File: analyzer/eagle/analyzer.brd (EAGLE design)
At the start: 33 x 38.1 mm, 34 parts, among them J4 USBSMD, U1 ATA6631, U2 FT232RL, U3 ATMEGA328, X1 16MHz

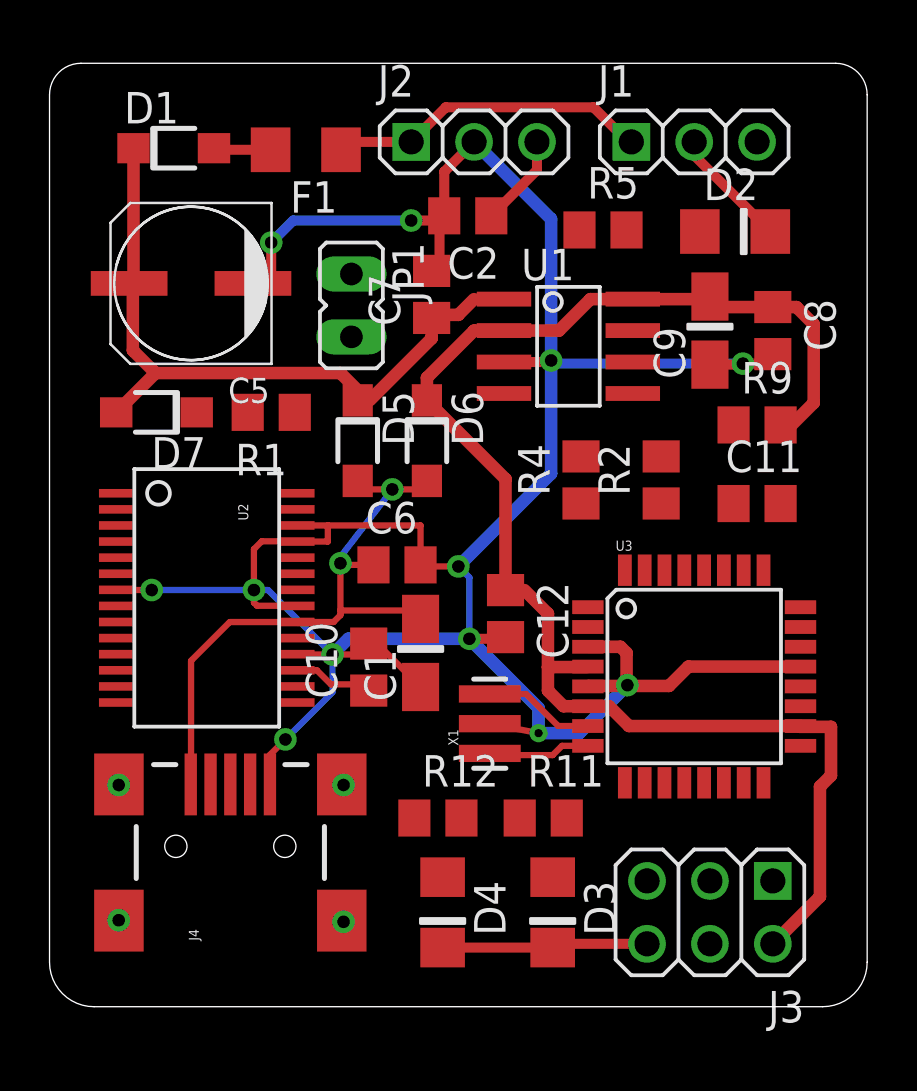
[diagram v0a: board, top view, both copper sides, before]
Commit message: Completed the routing of the analyzer board.
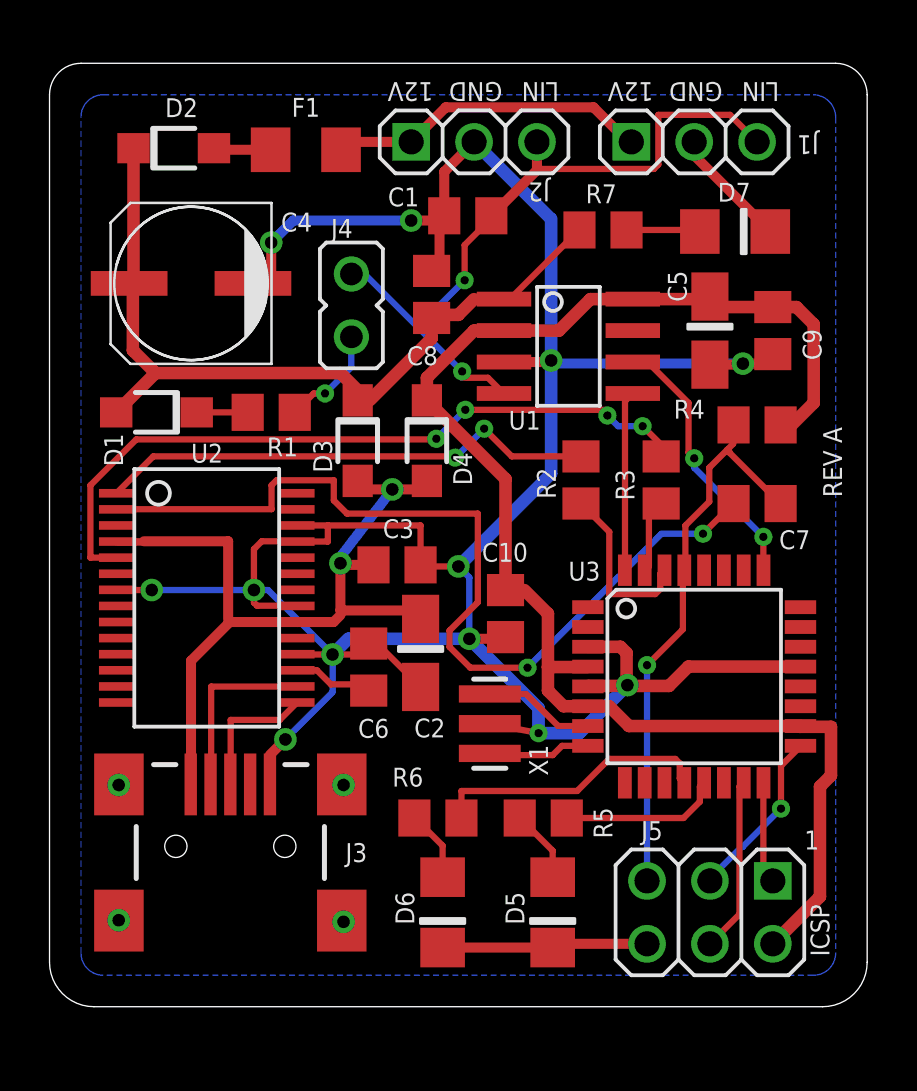
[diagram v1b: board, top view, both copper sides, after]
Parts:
- removed C11, C12: 0.1uF, analyzer:C0805
- removed JP1: (no value), jumper:JP1
- removed R11: 3.3K, analyzer:R0805
- removed R9: 10k, analyzer:R0805
- added C3: 0.1uF, analyzer:C0805
- added C4: 22uF 40V, analyzer:UD-6,3X5,8_NICHICON
- added J5: (no value), analyzer:2X03
- added R3, R7: 10K, analyzer:R0805
- C1: value 10uF -> 220pF; device analyzer:A/3216-18R -> analyzer:C0805
- C2: value 220pF -> 10uF; device analyzer:C0805 -> analyzer:A/3216-18R
- C5: value 22uF 40V -> 10uF; device analyzer:UD-6,3X5,8_NICHICON -> analyzer:A/3216-18R
- C7: value 0.1uF 50V -> 0.1uF
- C8: value 0.1uF -> 0.1uF 50V
- C9: value 10uF -> 0.1uF; device analyzer:A/3216-18R -> analyzer:C0805
- D2, D3: value RED -> MBR0540; device analyzer:1206-LED -> analyzer:SOD123FL
- D4: value GREEN -> MBR0540; device analyzer:1206-LED -> analyzer:SOD123FL
- D5, D7: value MBR0540 -> RED; device analyzer:SOD123FL -> analyzer:1206-LED
- D6: value MBR0540 -> GREEN; device analyzer:SOD123FL -> analyzer:1206-LED
- J3: value (none) -> USBSMD; device analyzer:2X03 -> analyzer:USB-MINIB
- J4: value USBSMD -> (none); device analyzer:USB-MINIB -> analyzer:JP1
- R4: value 10K -> 10k
- R5: value 10K -> 3.3K
- moved D7 24.5 mm to (27.7, 31.3), turned to 0 degrees
- moved R5 23.9 mm to (19.9, 7.62)
- moved D2 22.9 mm to (5.02, 34.7)
- moved J4 22.4 mm to (12.2, 28.3), turned to 180 degrees
- moved C5 21.0 mm to (26.7, 27.3), turned to 90 degrees
- moved D3 20.6 mm to (12.4, 22.9)
- moved D5 20.6 mm to (20.3, 3.81)
- moved J3 19.6 mm to (7.30, 6.48), turned to 90 degrees
- moved D4 19.1 mm to (15.2, 22.9)
- moved D6 19.1 mm to (15.9, 3.81)
- moved C1 17.8 mm to (16.9, 31.9), turned to 180 degrees
- moved C2 17.8 mm to (15.0, 14.3), turned to 90 degrees
- moved C7 15.6 mm to (28.6, 20.3), turned to 0 degrees
- moved C8 13.9 mm to (15.4, 28.8), turned to 90 degrees
- moved D1 10.7 mm to (4.32, 24.0), turned to 180 degrees
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- renumbered R12 to R6
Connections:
- net +12V: now also C4.+, C8.1, D1.A, D2.C, D3.C, R7.1; no longer C5.+, C7.1, D1.C, D5.C, D7.A, R5.1
- net +5V: now also C10.1, C5.+, C9.1, D4.C, J5.2, R4.2; no longer C12.1, C8.1, C9.+, D6.C, J3.2, R9.2
- net ERROR_LED: now also R5.2; no longer R11.2
- net GND: now also C1.2, C2.-, C3.2, C4.-, C9.2, D5.C, D6.C, D7.C, J3.5, J5.6; no longer C1.-, C12.2, C2.2, C7.2, C9.-, D2.C, D3.C, D4.C, J3.6, J4.5
- net LIN: now also C1.1, J4.1; no longer C2.1, JP1.1
- net MISO/LIN_DATA: now also J5.1; no longer J3.1
- net MOSI/LIN_ERR: now also J5.4; no longer J3.4
- net N$10: now also J3.3; no longer J4.3
- net N$11: now also C7.1; no longer C11.1
- net N$12: now also C2.+, C3.1, D3.A, D4.A, J3.1; no longer C1.+, C6.1, D5.A, D6.A, J4.1
- net N$13: now also R2.2; no longer R4.2
- net N$15: now also J3.2; no longer J4.2
- net N$16: now also C6.1; no longer C10.1
- net N$17: now also D7.A, R7.2; no longer D2.A, R5.2
- net N$3: now also D6.A; no longer D4.A
- net N$4: now also D5.A, R5.1; no longer D3.A, R11.1
- net N$5: now also R3.2; no longer R2.2
- net N$6: now also D2.A; no longer D1.A
- net N$8: now also D1.C; no longer D7.C
- net N$9: now also J4.2; no longer JP1.2
- net RESET: now also C7.2, J5.5, R4.1; no longer C11.2, J3.5, R9.1
- net SCK: now also J5.3; no longer J3.3
- net SER_RX: now also R2.1; no longer R4.1
- net SER_TX: now also R3.1; no longer R2.1
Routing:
- net N$11: track 0.00 -> 37.1 mm, vias 0 -> 2
- net N$5: track 0.00 -> 29.5 mm, vias 0 -> 4
- net LIN: track 3.75 -> 29.2 mm, vias 0 -> 2
- net RESET: track 0.00 -> 22.9 mm, vias 0 -> 1
- net N$13: track 0.00 -> 20.4 mm, vias 0 -> 2
- net FRAME_LED: track 0.00 -> 11.4 mm
- net LIN_TX: track 0.00 -> 10.9 mm, vias 0 -> 2
- net N$12: track 25.4 -> 33.3 mm
- net N$15: track 0.00 -> 7.45 mm
- net LIN_RX: track 0.00 -> 7.28 mm
- net SER_RX: track 0.00 -> 7.12 mm
- net MOSI/LIN_ERR: track 0.00 -> 7.08 mm
- net SCK: track 0.00 -> 7.00 mm, vias 0 -> 1
- net ERROR_LED: track 0.00 -> 6.49 mm
- net N$10: track 0.00 -> 5.59 mm
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- added copper zone on layer 16, net GND
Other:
- board text added: "1"
- board text added: "12V"
- board text added: "GND"
- board text added: "ICSP"
- board text added: "LIN"
- board text added: "LINBUS ANALYZER"
- board text added: "REV A"

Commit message: Analyzer board layout completed.
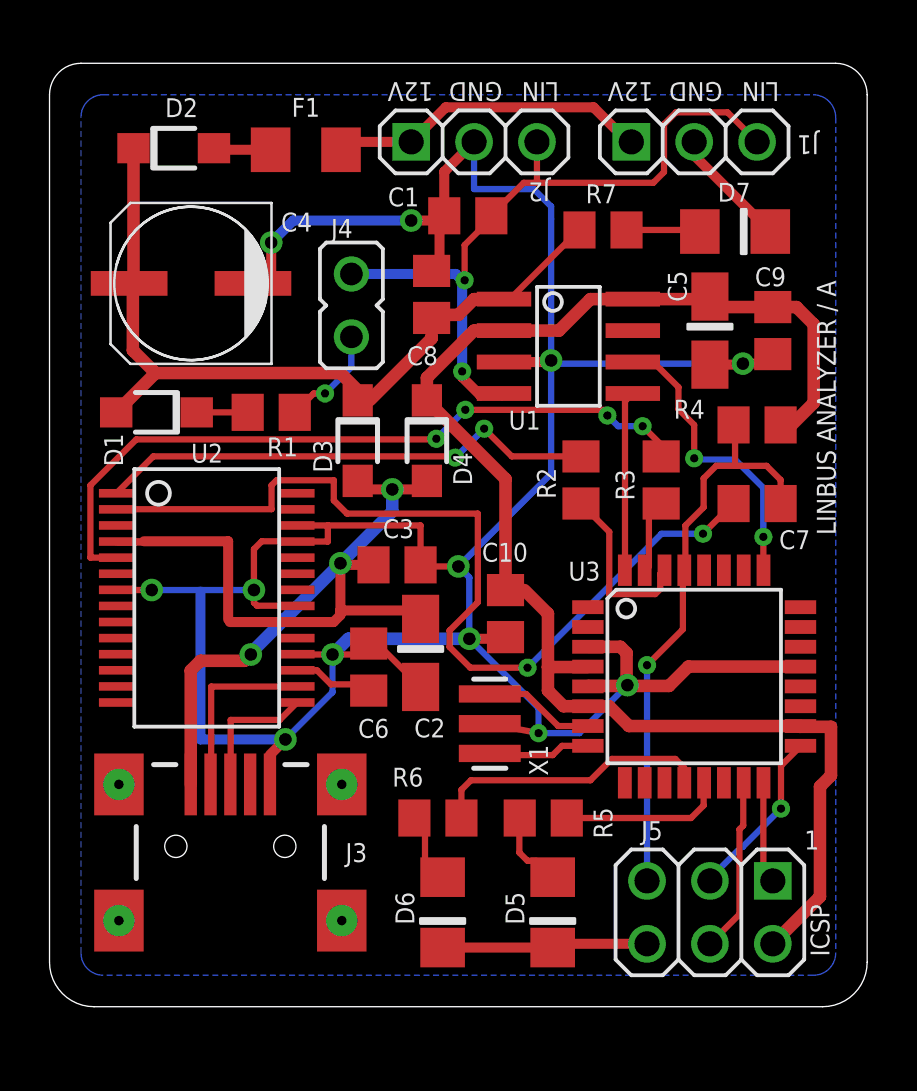
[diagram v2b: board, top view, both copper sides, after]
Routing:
- net GND: track 132.7 -> 139.3 mm
- net N$12: track 33.3 -> 38.7 mm, vias 2 -> 3
- net LIN_TX: track 10.9 -> 12.0 mm
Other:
- board text added: "LINBUS ANALYZER / A"
- board text removed: "LINBUS ANALYZER"
- board text removed: "REV A"

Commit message: Added analyzer flash image.
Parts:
- R1: value 10K -> 1K
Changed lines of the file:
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@@
 <attribute name="VALUE" x="6.318" y="26.503" size="1.27" layer="27" rot="R180"/>
 </element>
-<element name="R1" library="analyzer" package="R0805" value="10K" x="8.9535" y="24.003" smashed="yes" rot="R180">
+<element name="R1" library="analyzer" package="R0805" value="1K" x="8.9535" y="24.003" smashed="yes" rot="R180">
 <attribute name="NAME" x="10.033" y="22.987" size="0.762" layer="25" rot="R180"/>
 <attribute name="VALUE" x="9.5885" y="26.543" size="1.27" layer="27" rot="R180"/>

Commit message: Added Analyzer bom.
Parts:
- F1: value 250ma slow -> 500ma slow
- R4: value 10k -> 10K
- R6: value 3.3k -> 3.3K
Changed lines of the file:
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@@
 <attribute name="VALUE" x="19.304" y="5.08" size="1.27" layer="27"/>
 </element>
-<element name="R6" library="analyzer" package="R0805" value="3.3k" x="15.6845" y="7.62" smashed="yes">
+<element name="R6" library="analyzer" package="R0805" value="3.3K" x="15.6845" y="7.62" smashed="yes">
 <attribute name="NAME" x="13.843" y="8.89" size="0.762" layer="25"/>
 <attribute name="VALUE" x="15.0495" y="5.08" size="1.27" layer="27"/>
@@
 <attribute name="VALUE" x="17.9705" y="27.4955" size="1.27" layer="27" rot="R90"/>
 </element>
-<element name="F1" library="analyzer" package="1206" value="250ma slow" x="10.3505" y="34.6075" smashed="yes" rot="R180">
+<element name="F1" library="analyzer" package="1206" value="500ma slow" x="10.3505" y="34.6075" smashed="yes" rot="R180">
 <attribute name="NAME" x="9.779" y="35.941" size="0.762" layer="25"/>
 <attribute name="VALUE" x="11.6205" y="37.1475" size="1.27" layer="27" rot="R180"/>
@@
 <attribute name="VALUE" x="28.995" y="25.355" size="1.27" layer="27" rot="R90"/>
 </element>
-<element name="R4" library="analyzer" package="R0805" value="10k" x="28.575" y="23.495" smashed="yes">
+<element name="R4" library="analyzer" package="R0805" value="10K" x="28.575" y="23.495" smashed="yes">
 <attribute name="NAME" x="25.2095" y="23.749" size="0.762" layer="25"/>
 <attribute name="VALUE" x="27.94" y="20.955" size="1.27" layer="27"/>

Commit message: Harmonized the design of the three boards. Changed the beepr configuration button sequence (ignition on, 6 clicks, ignition off).
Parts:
- D7: value RED -> BLUE
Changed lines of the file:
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@@
 <attribute name="VALUE" x="17.311" y="12.3375" size="1.27" layer="27" rot="R90"/>
 </element>
-<element name="D7" library="analyzer" package="1206-LED" value="RED" x="27.686" y="31.3055" smashed="yes">
+<element name="D7" library="analyzer" package="1206-LED" value="BLUE" x="27.686" y="31.3055" smashed="yes">
 <attribute name="NAME" x="26.9875" y="32.512" size="0.762" layer="25"/>
 <attribute name="VALUE" x="26.416" y="28.7655" size="1.27" layer="27"/>
